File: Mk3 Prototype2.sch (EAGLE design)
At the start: 189 parts, among them IC1 BD49XXX, IC2 NCP1529MU, IC3 STM32F401V, IC4 CC3100, IC5 S25FL216K0PMFI011, IC6 CC3100MOD, J1 ZX62-AB-5PA(11), J2 ER-TFT024-3, J3 SWD_SHROUD, Q1 DMMT5401, Q2 NTR4101, Q3 NTR4101, Q5 NTR4101, Q6 NTR4101, SW1 JOYSTICK_MINI_MULTICOMP, U3 MCP73831, U4 USD-SOCKETNEW, X1 ESP-07, X2 CRYSTAL-3.2-2.5, X3 ABS07-32.768KHZ-T, X4 DNP - ABS07-32.768KHZ-T, X5 Q24FA20H00396, X6 MC-921

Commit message: moved bits around, changed outline
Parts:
- C20, C21: value 0402/6.2p/50V/NP0 -> 0402/10p/50V/NP0
- R1: device TiLDA Mk3 Parts:R-EU_0603K-SMALL -> TiLDA Mk3 Parts:R-EU_0207/10
- TP1, TP10, TP2, TP3, TP4, TP5, TP6, TP7, TP8, TP9: value TP4MM -> TP3MM; device TiLDA Mk3 Parts:TP4MM -> TiLDA Mk3 Parts:TP3MM
- X2: value CRYSTAL-3.2-2.5 -> 16MHz-3.2-2.5
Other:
- note added: "SRN2512-2R2M"
- note added: "buzzer, accel footprint?"
- note added: "consider better switches"
- note added: "wrong package"
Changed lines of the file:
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@@
 <?xml version="1.0" encoding="utf-8"?>
 <!DOCTYPE eagle SYSTEM "eagle.dtd">
-<eagle version="6.6.0">
+<eagle version="7.1.0">
 <drawing>
 <settings>
@@
 <part name="R23" library="TiLDA Mk3 Parts" deviceset="R-EU_" device="0603K-SMALL" value="0402/22/1%"/>
 <part name="R25" library="TiLDA Mk3 Parts" deviceset="R-EU_" device="0603K-SMALL" value="0402/22/1%"/>
-<part name="X2" library="TiLDA Mk3 Parts" deviceset="CRYSTAL" device="-3.2-2.5" value="CRYSTAL-3.2-2.5"/>
+<part name="X2" library="TiLDA Mk3 Parts" deviceset="CRYSTAL" device="-3.2-2.5" value="16MHz-3.2-2.5"/>
 <part name="GND54" library="TiLDA Mk3 Parts" deviceset="GND" device=""/>
 <part name="GND55" library="TiLDA Mk3 Parts" deviceset="GND" device=""/>
-<part name="C21" library="TiLDA Mk3 Parts" deviceset="C-EU" device="C0603K-SMALL" value="0402/6.2p/50V/NP0"/>
-<part name="C20" library="TiLDA Mk3 Parts" deviceset="C-EU" device="C0603K-SMALL" value="0402/6.2p/50V/NP0"/>
+<part name="C21" library="TiLDA Mk3 Parts" deviceset="C-EU" device="C0603K-SMALL" value="0402/10p/50V/NP0"/>
+<part name="C20" library="TiLDA Mk3 Parts" deviceset="C-EU" device="C0603K-SMALL" value="0402/10p/50V/NP0"/>
 <part name="GND58" library="TiLDA Mk3 Parts" deviceset="GND" device=""/>
 <part name="R6" library="TiLDA Mk3 Parts" deviceset="R-EU_" device="0603K-SMALL" value="0402/2k/5%"/>
@@
 <part name="GND68" library="TiLDA Mk3 Parts" deviceset="GND" device=""/>
 <part name="GND69" library="TiLDA Mk3 Parts" deviceset="GND" device=""/>
-<part name="TP3" library="TiLDA Mk3 Parts" deviceset="TP" device="4MM"/>
-<part name="TP1" library="TiLDA Mk3 Parts" deviceset="TP" device="4MM"/>
-<part name="TP2" library="TiLDA Mk3 Parts" deviceset="TP" device="4MM"/>
-<part name="TP4" library="TiLDA Mk3 Parts" deviceset="TP" device="4MM"/>
-<part name="TP8" library="TiLDA Mk3 Parts" deviceset="TP" device="4MM"/>
-<part name="TP5" library="TiLDA Mk3 Parts" deviceset="TP" device="4MM"/>
+<part name="TP3" library="TiLDA Mk3 Parts" deviceset="TP" device="3MM" value="TP3MM"/>
+<part name="TP1" library="TiLDA Mk3 Parts" deviceset="TP" device="3MM" value="TP3MM"/>
+<part name="TP2" library="TiLDA Mk3 Parts" deviceset="TP" device="3MM" value="TP3MM"/>
+<part name="TP4" library="TiLDA Mk3 Parts" deviceset="TP" device="3MM" value="TP3MM"/>
+<part name="TP8" library="TiLDA Mk3 Parts" deviceset="TP" device="3MM" value="TP3MM"/>
+<part name="TP5" library="TiLDA Mk3 Parts" deviceset="TP" device="3MM" value="TP3MM"/>
 <part name="R18" library="TiLDA Mk3 Parts" deviceset="R-EU_" device="0603K-SMALL" value="0402/220k/5%"/>
 <part name="R19" library="TiLDA Mk3 Parts" deviceset="R-EU_" device="0603K-SMALL" value="0402/220k/5%"/>
@@
 <part name="GND74" library="TiLDA Mk3 Parts" deviceset="GND" device=""/>
 <part name="GND75" library="TiLDA Mk3 Parts" deviceset="GND" device=""/>
-<part name="TP6" library="TiLDA Mk3 Parts" deviceset="TP" device="4MM"/>
-<part name="TP9" library="TiLDA Mk3 Parts" deviceset="TP" device="4MM"/>
-<part name="TP10" library="TiLDA Mk3 Parts" deviceset="TP" device="4MM"/>
+<part name="TP6" library="TiLDA Mk3 Parts" deviceset="TP" device="3MM" value="TP3MM"/>
+<part name="TP9" library="TiLDA Mk3 Parts" deviceset="TP" device="3MM" value="TP3MM"/>
+<part name="TP10" library="TiLDA Mk3 Parts" deviceset="TP" device="3MM" value="TP3MM"/>
 <part name="GND78" library="TiLDA Mk3 Parts" deviceset="GND" device=""/>
 <part name="GND79" library="TiLDA Mk3 Parts" deviceset="GND" device=""/>
@@
 <part name="SJ2" library="TiLDA Mk3 Parts" deviceset="SOLDERJUMPER" device="TRACE"/>
 <part name="LED1" library="TiLDA Mk3 Parts" deviceset="LED" device="5MM"/>
-<part name="R1" library="TiLDA Mk3 Parts" deviceset="R-EU_" device="0603K-SMALL"/>
+<part name="R1" library="TiLDA Mk3 Parts" deviceset="R-EU_" device="0207/10"/>
 <part name="Q5" library="TiLDA Mk3 Parts" deviceset="MOSFET-P" device="-SOT23" value="NTR4101"/>
 <part name="GND105" library="TiLDA Mk3 Parts" deviceset="GND" device=""/>
@@
 <part name="ANT2" library="TiLDA Mk3 Parts" deviceset="CHIPANT" device=""/>
 <part name="S7" library="SparkFun-Electromechanical" deviceset="SWITCH-MOMENTARY-2" device="SMD-1101NE"/>
-<part name="TP7" library="TiLDA Mk3 Parts" deviceset="TP" device="4MM"/>
+<part name="TP7" library="TiLDA Mk3 Parts" deviceset="TP" device="3MM" value="TP3MM"/>
 <part name="IC6" library="TiLDA Mk3 Parts" deviceset="CC3100MOD" device=""/>
 <part name="ANT1" library="TiLDA Mk3 Parts" deviceset="CHIPANT" device=""/>
@@
 <text x="612.14" y="264.16" size="1.778" layer="90">http://processors.wiki.ti.com/index.php/CC3100_Production_Line_Guide#Programming_the_CC3100_QFN_in_the_Production_Line</text>
 <text x="797.56" y="127" size="2.54" layer="90">aref arrangment, consider to allow Aref changing on gpio</text>
-<text x="589.28" y="114.3" size="1.778" layer="91">spec</text>
+<text x="589.28" y="114.3" size="1.778" layer="91">SRN2512-2R2M</text>
 <text x="627.38" y="76.2" size="1.778" layer="91">close for OTG</text>
 <text x="86.36" y="109.22" size="1.778" layer="91">/ JOY_CEN</text>
@@
 <wire x1="660.4" y1="78.74" x2="660.4" y2="45.72" width="0.1524" layer="97"/>
 <wire x1="660.4" y1="45.72" x2="640.08" y2="45.72" width="0.1524" layer="97"/>
+<text x="586.74" y="119.38" size="1.778" layer="91">wrong package</text>
+<text x="525.78" y="111.76" size="1.778" layer="91">wrong package</text>
+<text x="358.14" y="114.3" size="1.778" layer="91" rot="R180">consider better switches</text>
+<text x="797.56" y="213.36" size="2.54" layer="90">buzzer, accel footprint?</text>
 </plain>
 <instances>

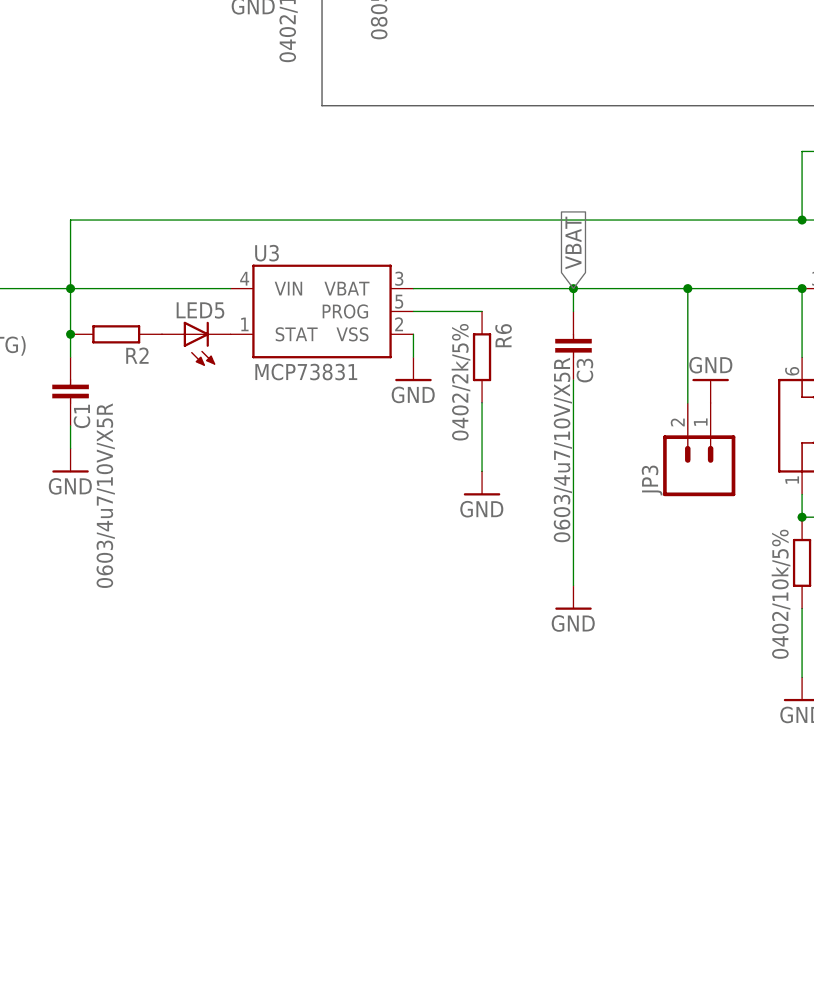
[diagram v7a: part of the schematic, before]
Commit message: started adding battery protection uc
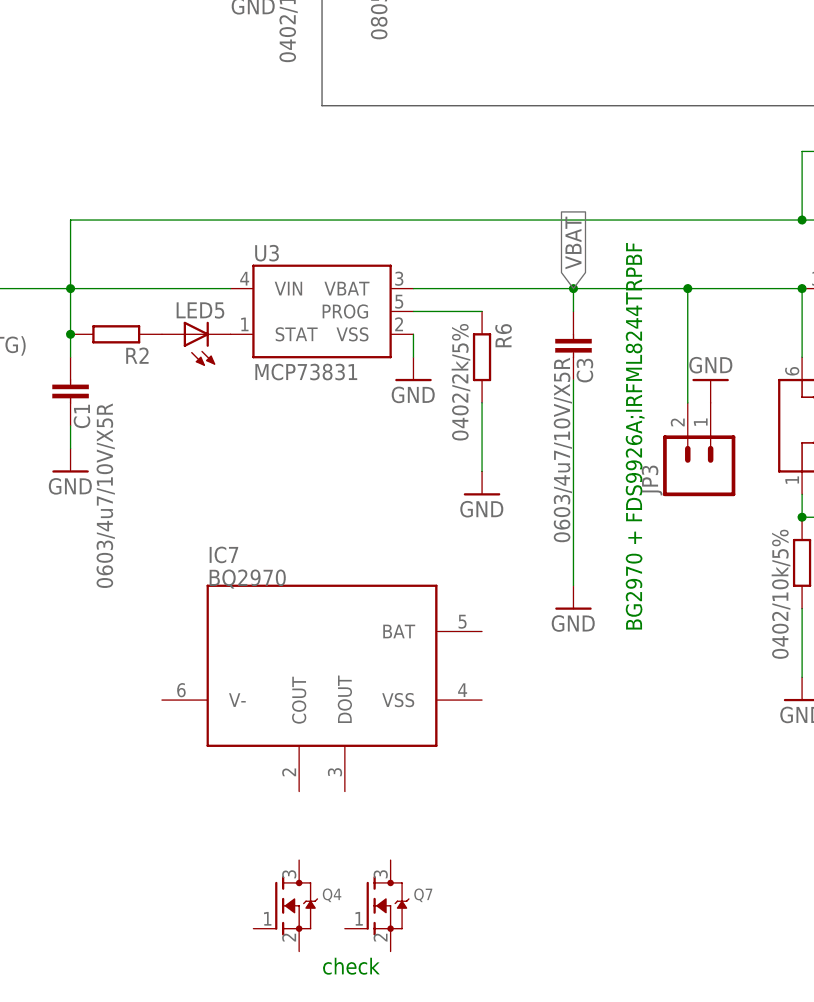
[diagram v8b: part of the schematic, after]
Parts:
- added IC7: BQ2970, TiLDA Mk3 Parts:BQ2970
- added Q4, Q7: (no value), TiLDA Mk3 Parts:MOSFET-N-SOT23-SPARK
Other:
- note added: "BG2970 + FDS9926A;IRFML8244TRPBF"
- note added: "check"
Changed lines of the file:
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@@
 <part name="JP1" library="TiLDA Mk3 Parts" deviceset="M10" device="NOSILK"/>
 <part name="JP2" library="TiLDA Mk3 Parts" deviceset="M10" device="NOSILK"/>
+<part name="IC7" library="TiLDA Mk3 Parts" deviceset="BQ2970" device=""/>
+<part name="Q4" library="TiLDA Mk3 Parts" deviceset="MOSFET-N" device="-SOT23-SPARK"/>
+<part name="Q7" library="TiLDA Mk3 Parts" deviceset="MOSFET-N" device="-SOT23-SPARK"/>
 </parts>
 <sheets>
@@
 <text x="358.14" y="114.3" size="1.778" layer="91" rot="R180">consider better switches</text>
 <text x="797.56" y="213.36" size="2.54" layer="90">buzzer, accel footprint?</text>
+<text x="589.28" y="20.32" size="1.778" layer="91" rot="R90">BG2970 + FDS9926A;IRFML8244TRPBF</text>
+<text x="553.72" y="-17.78" size="1.778" layer="91">check</text>
 </plain>
 <instances>
@@
 <attribute name="NAME" x="347.98" y="26.67" size="1.778" layer="95" rot="R180"/>
 </instance>
+<instance part="IC7" gate="G$1" x="563.88" y="17.78"/>
+<instance part="Q4" gate="G$1" x="548.64" y="-10.16"/>
+<instance part="Q7" gate="G$1" x="558.8" y="-10.16"/>
 </instances>
 <busses>
